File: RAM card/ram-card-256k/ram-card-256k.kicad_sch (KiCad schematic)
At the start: 12 parts, among them J1 RAM card connector, U1 HC138, U2 KM681000BLG, U3 KM681000BLG

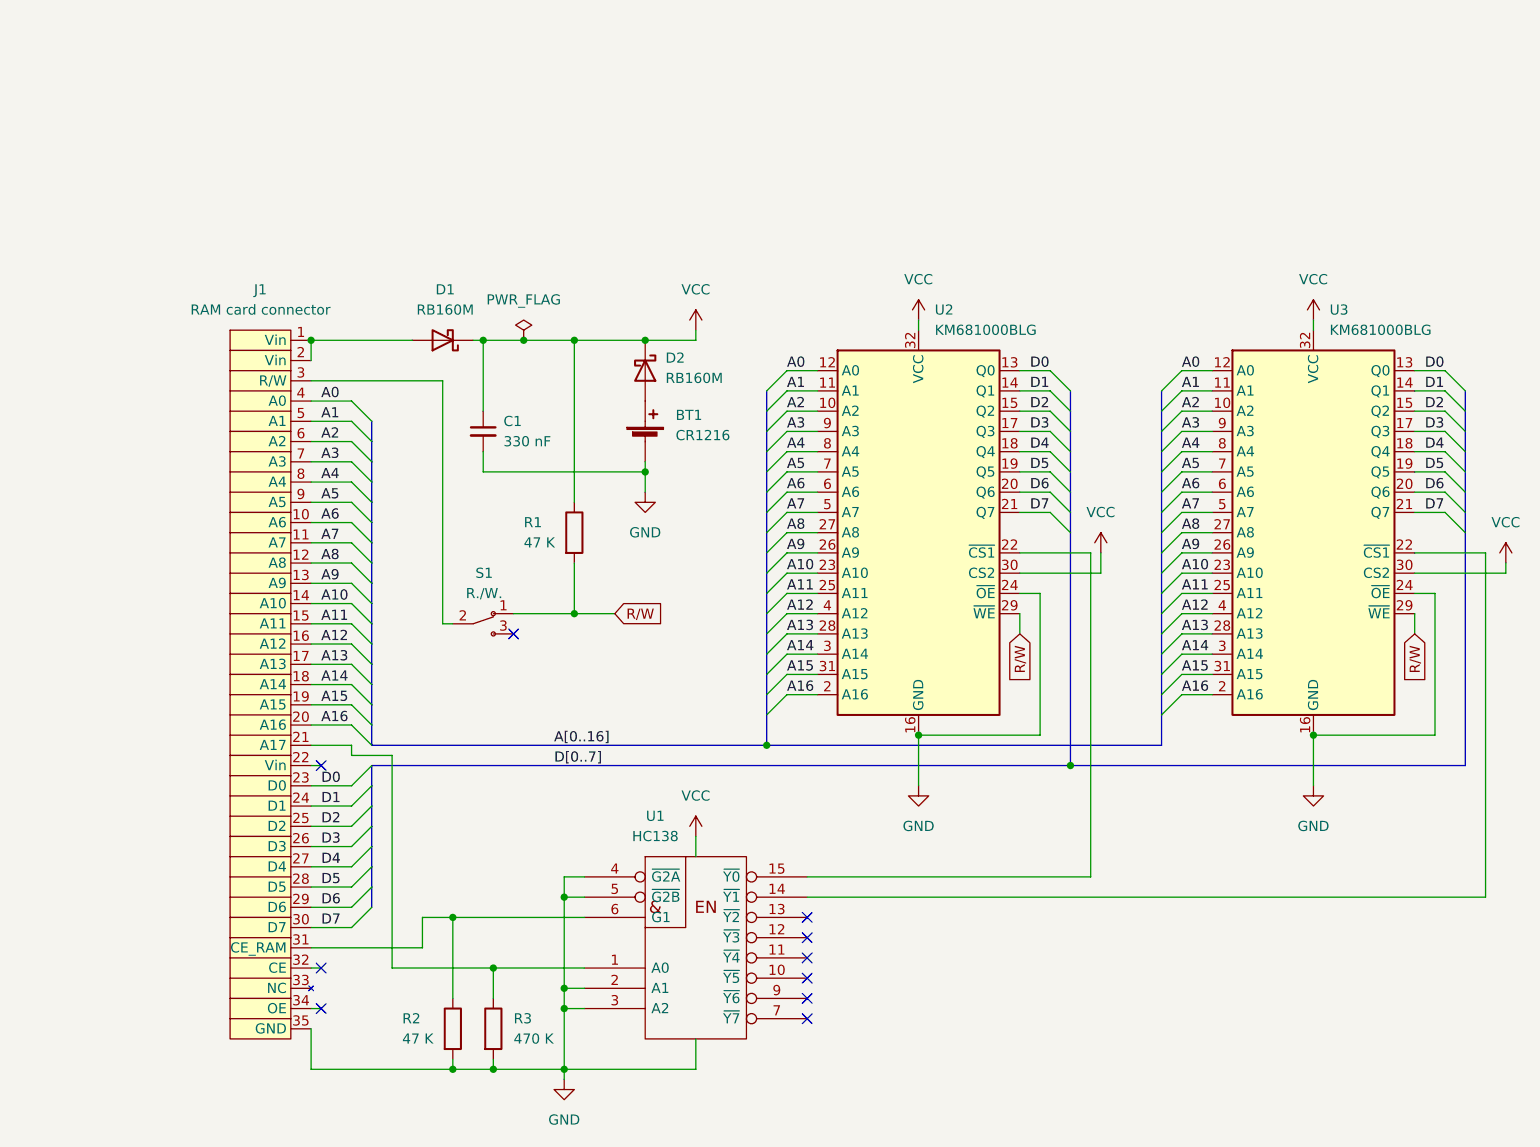
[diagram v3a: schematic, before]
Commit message: Improve footprints
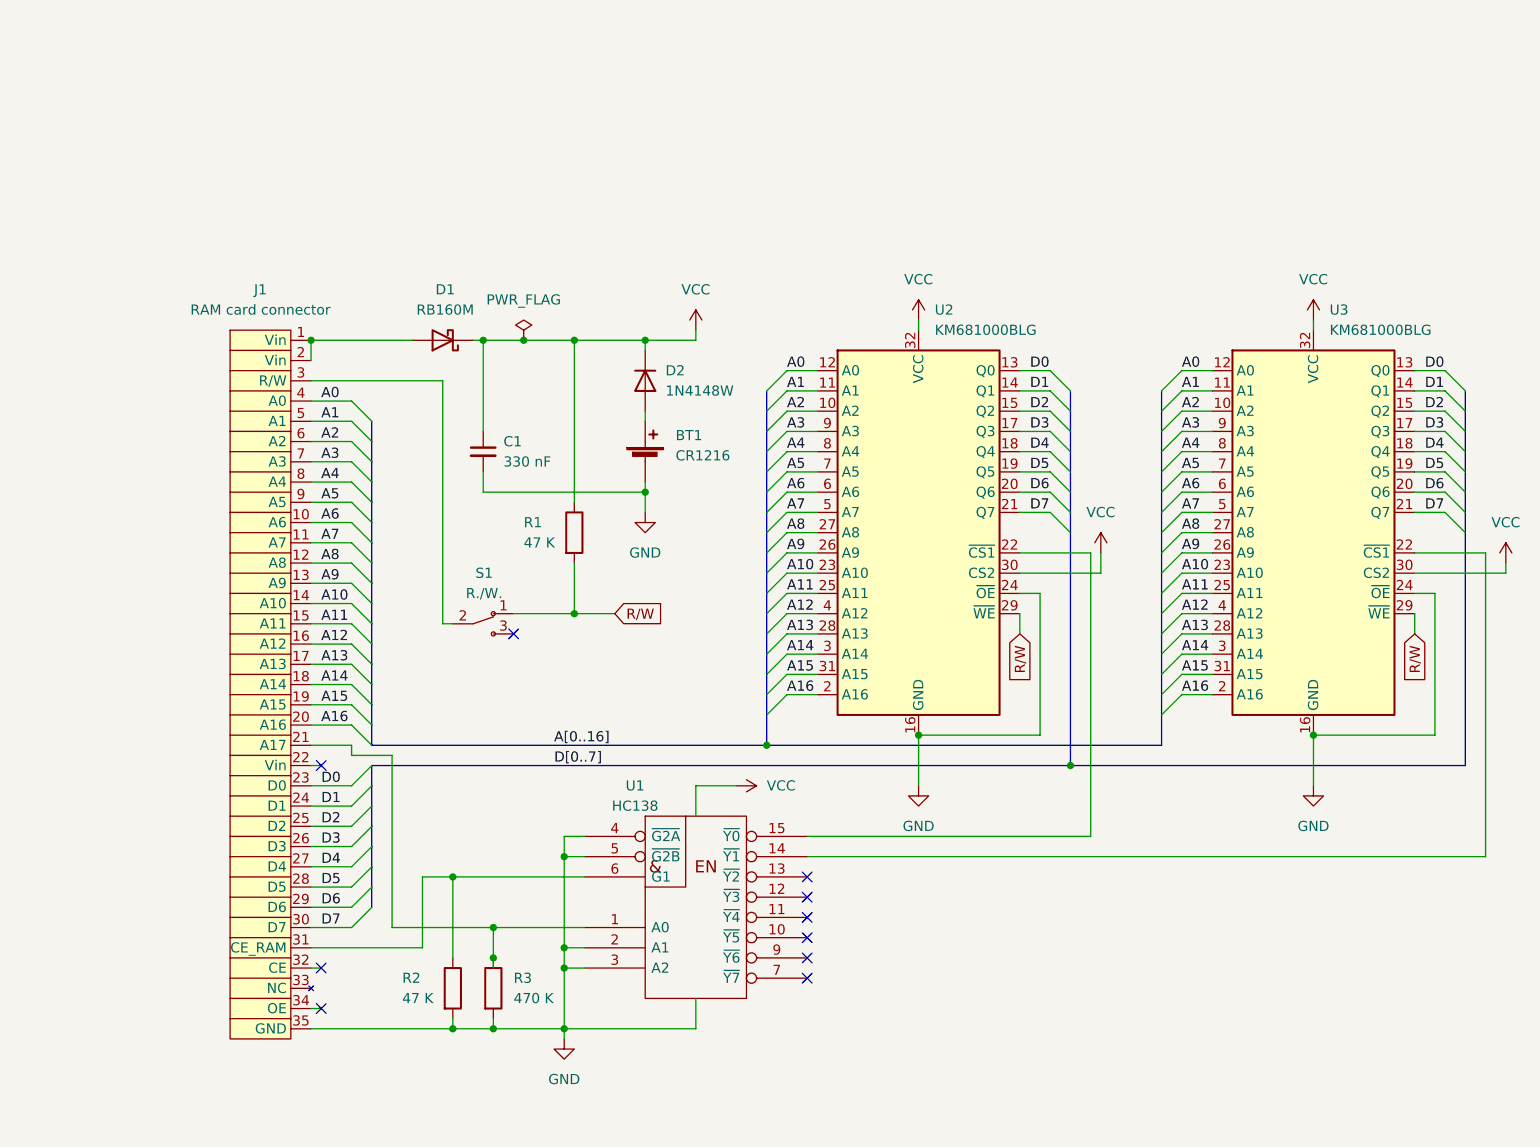
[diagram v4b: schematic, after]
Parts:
- removed D2: RB160M, Diode_SMD:D_SOD-123, symbol Device:D_Schottky
- added D2: 1N4148W, Diode_SMD:D_SOD-123, symbol Diode:1N4148W
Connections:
- net VCC: now also D2.1 (K)
- net at BT1.1 (+): now also D2.2 (A)
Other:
- moved on the sheet: BT1, C1, R2, R3, U1

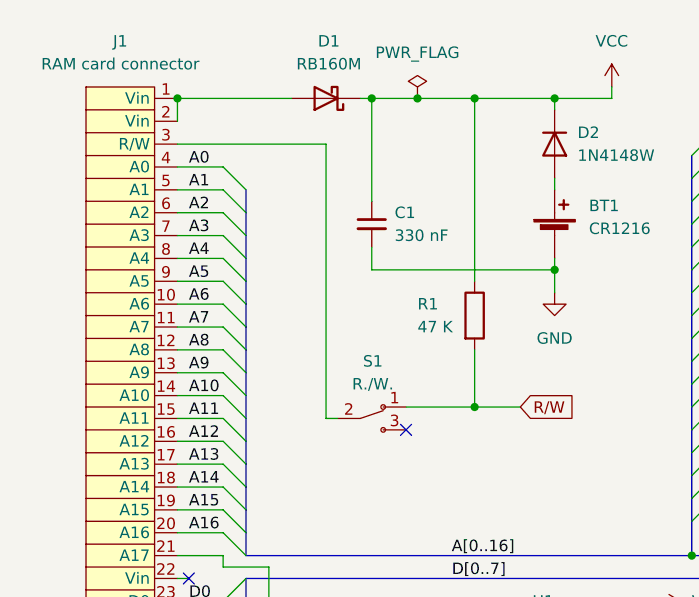
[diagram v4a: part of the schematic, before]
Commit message: Component layout
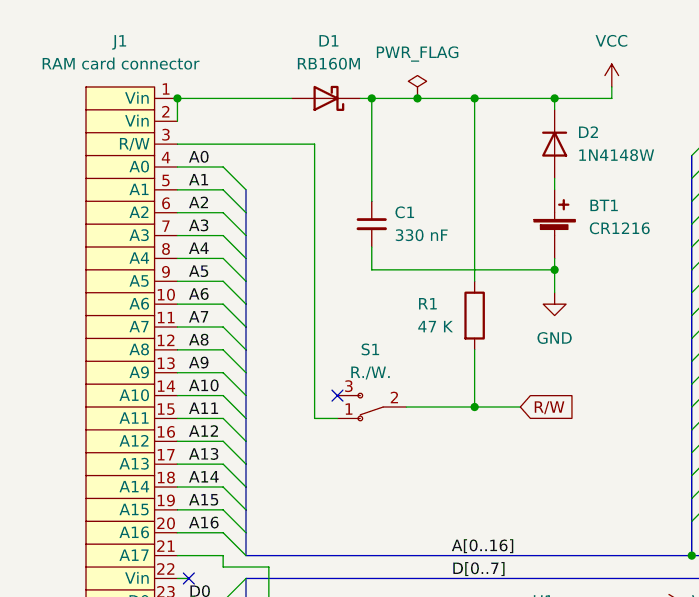
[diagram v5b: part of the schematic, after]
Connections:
- net R/W: now also S1.2; no longer S1.1
- net at J1.3 (R/W): now also S1.1; no longer S1.2
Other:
- moved on the sheet: S1
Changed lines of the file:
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@@
   (no_connect (at 144.78 124.46))
   (no_connect (at 144.78 121.92))
-  (no_connect (at 107.95 91.44))
+  (no_connect (at 100.33 87.63))
   (no_connect (at 83.82 133.35))
   (no_connect (at 83.82 138.43))
@@
     (stroke (width 0) (type default) (color 0 0 0 0))
   )
-  (wire (pts (xy 99.06 59.69) (xy 99.06 90.17))
+  (wire (pts (xy 97.79 59.69) (xy 97.79 90.17))
     (stroke (width 0) (type default) (color 0 0 0 0))
   )
@@
     (stroke (width 0) (type default) (color 0 0 0 0))
   )
-  (wire (pts (xy 82.55 59.69) (xy 99.06 59.69))
+  (wire (pts (xy 82.55 59.69) (xy 97.79 59.69))
     (stroke (width 0) (type default) (color 0 0 0 0))
   )
@@
     (stroke (width 0) (type default) (color 0 0 0 0))
   )
-  (wire (pts (xy 99.06 90.17) (xy 100.33 90.17))
+  (wire (pts (xy 97.79 90.17) (xy 100.33 90.17))
     (stroke (width 0) (type default) (color 0 0 0 0))
   )
@@
     (pin "2")
   )
-  (symbol (lib_id "custom-symbols:Slider_switch") (at 105.41 83.82 0) (unit 1)
-    (in_bom yes) (on_board yes) (fields_autoplaced)
-    (property "Reference" "S1" (id 0) (at 104.267 83.82 0))
-    (property "Value" "R./W." (id 1) (at 104.267 86.36 0))
-    (property "Footprint" "custom-footprints:slider_switch_7x3" (id 2) (at 105.41 83.82 0)
-      (effects (font (size 1.27 1.27)) hide)
-    )
-    (property "Datasheet" "" (id 3) (at 105.41 83.82 0)
-      (effects (font (size 1.27 1.27)) hide)
-    )
+  (symbol (lib_id "custom-symbols:Slider_switch") (at 102.87 95.25 180) (unit 1)
+    (in_bom yes) (on_board yes) (fields_autoplaced)
+    (property "Reference" "S1" (id 0) (at 104.013 82.55 0))
+    (property "Value" "R./W." (id 1) (at 104.013 85.09 0))
+    (property "Footprint" "custom-footprints:slider_switch_7x3" (id 2) (at 102.87 95.25 0)
+      (effects (font (size 1.27 1.27)) hide)
+    )
+    (property "Datasheet" "" (id 3) (at 102.87 95.25 0)
+      (effects (font (size 1.27 1.27)) hide)
+    )

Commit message: Layout
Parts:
- U1: footprint Package_SO:SOP-16_4.55x10.3mm_P1.27mm -> Package_SO:SOP-16_3.9x9.9mm_P1.27mm
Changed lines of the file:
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@@
     (property "Reference" "U1" (id 0) (at 123.19 110.49 0))
     (property "Value" "HC138" (id 1) (at 123.19 113.03 0))
-    (property "Footprint" "Package_SO:SOP-16_4.55x10.3mm_P1.27mm" (id 2) (at 130.81 121.92 0)
-      (effects (font (size 1.27 1.27)) hide)
-    )
+    (property "Footprint" "Package_SO:SOP-16_3.9x9.9mm_P1.27mm" (id 2) (at 130.81 121.92 0))
     (property "Datasheet" "" (id 3) (at 130.81 121.92 0)
       (effects (font (size 1.27 1.27)) hide)
@@
     )
     (path "/7250dad1-b103-48a6-bef8-ebcb905dca40"
-      (reference "U1") (unit 1) (value "HC138") (footprint "Package_SO:SOP-16_4.55x10.3mm_P1.27mm")
+      (reference "U1") (unit 1) (value "HC138") (footprint "Package_SO:SOP-16_3.9x9.9mm_P1.27mm")
     )
     (path "/0b1a0680-7430-4b0f-aaa1-4269f0df11fa"

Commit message: Version 1.0
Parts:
- BT1: footprint custom-footprints:Battery_CR1216 -> custom-footprints:Battery_CR1216_hole
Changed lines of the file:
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@@
       (effects (font (size 1.27 1.27)) (justify left))
     )
-    (property "Footprint" "custom-footprints:Battery_CR1216" (id 2) (at 124.46 68.326 90)
+    (property "Footprint" "custom-footprints:Battery_CR1216_hole" (id 2) (at 124.46 68.326 90)
       (effects (font (size 1.27 1.27)) hide)
     )
@@
     )
     (path "/d6c92ca2-7330-41ea-94a6-91aa589c8ef3"
-      (reference "BT1") (unit 1) (value "CR1216") (footprint "custom-footprints:Battery_CR1216")
+      (reference "BT1") (unit 1) (value "CR1216") (footprint "custom-footprints:Battery_CR1216_hole")
     )
     (path "/d5b91f7d-2204-491d-9121-28cfcffdb18d"

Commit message: Assign 3d-model
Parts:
- U1: footprint Package_SO:SOP-16_3.9x9.9mm_P1.27mm -> Package_SO:SOIC-16_3.9x9.9mm_P1.27mm
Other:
- title: (none) -> 256K RAM card for Sharp Pocket PC-E500 
- moved on the sheet: U2, U3
